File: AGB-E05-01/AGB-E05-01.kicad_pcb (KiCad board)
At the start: 2 copper layers, 51 x 31.1 mm, 24 parts, among them U0 CartBus, X1 Crystal_GND2

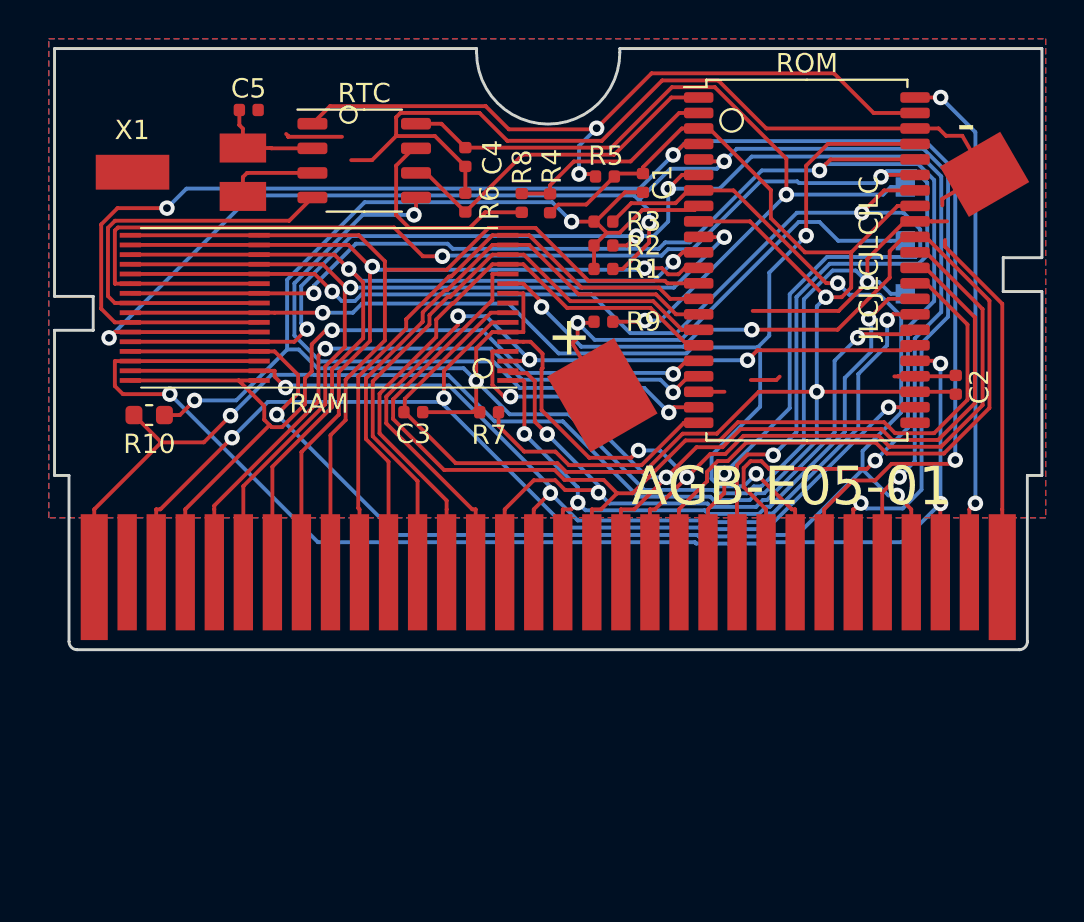
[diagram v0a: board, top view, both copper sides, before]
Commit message: Updated AGB-E05-01 to look more original
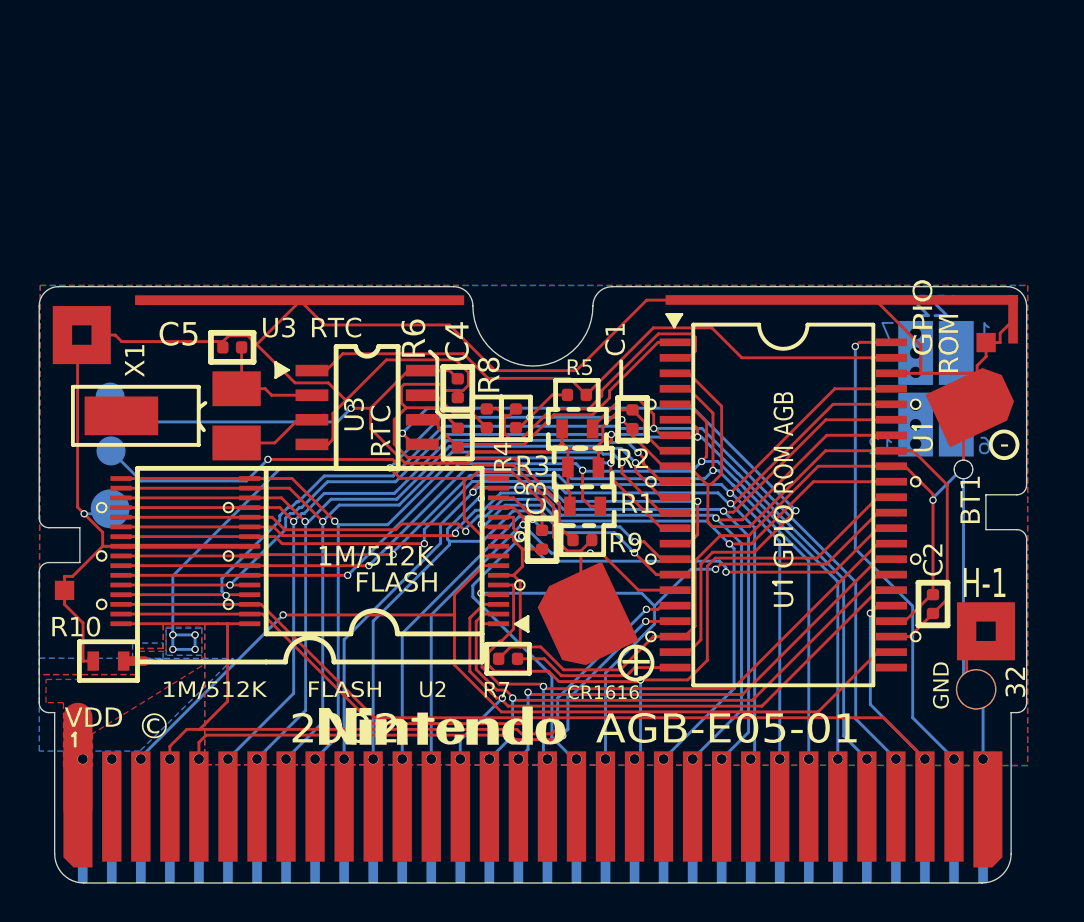
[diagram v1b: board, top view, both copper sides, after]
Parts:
- added A1: Date Indicator, HDR_Gameboy_Date_Indicators:06 June, B.Cu at (172.4, 88.2)
- added A2: 3x3Pad, HDR_Gameboy:3x3mm_Pad, F.Cu at (174.9, 100.7)
- added A3: 3x3Pad, HDR_Gameboy:3x3mm_Pad, F.Cu at (128.2, 85.4)
- added A4: 1x1Pad, HDR_Gameboy:1x1mm_Pad, F.Cu at (175.0, 85.8)
- added A5: 1x1Pad, HDR_Gameboy:1x1mm_Pad, F.Cu at (127.4, 98.6)
- added A6: CartBrow_Left, HDR_Gameboy:AGB-Cartbrow_Left, F.Cu at (139.5, 83.6)
- added A7: CartBrow_Right, HDR_Gameboy:AGB-Cartbrow_Right, F.Cu at (167.5, 83.6)
- added G1: Nintendo Logo, Custom:Nintendo-GBA-Logo, F.Cu at (146.9, 105.6)
- added PlatedHole1: MountingHole, Custom:TestPoint_Plated_Hole_D2.0mm, F.Cu at (174.4, 103.7)
- added kibuzzard-62A1ACD3: G***, kibuzzard-62A1ACD3, B.Cu at (130.4, 96.0)
- added kibuzzard-62A1AD16: G***, kibuzzard-62A1AD16, B.Cu at (131.6, 91.4)
- added kibuzzard-62A1AD21: G***, kibuzzard-62A1AD21, B.Cu at (131.6, 88.6)
- BT1: footprint NintendoFootprints:CR1616 -> HDR_Gameboy:AGB-CR1616
- C1, C2, C3, C4, C5: footprint Capacitor_SMD:C_0402_1005Metric -> HDR_Gameboy:AGB-C_0402
- R1, R2, R3: footprint Resistor_SMD:R_0402_1005Metric -> HDR_Gameboy:AGB-R-0603_OPT
- R10: footprint Resistor_SMD:R_0603_1608Metric -> HDR_Gameboy:AGB-R-0603
- R4, R5, R6, R7, R8, R9: footprint Resistor_SMD:R_0402_1005Metric -> HDR_Gameboy:AGB-R_0402
- TP1, TP2: footprint TestPoint:TestPoint_Pad_1.0x1.0mm -> HDR_Gameboy:AGB-Testpoint
- TP3: footprint TestPoint:TestPoint_Pad_1.0x1.0mm -> HDR_Gameboy:AGB-Testpoint_Ground
- U0: footprint NintendoFootprints:CartBus -> HDR_Gameboy:AGB_Cartridge
- U1: renamed from ROM; footprint Package_SO:TSOP-II-44_10.16x18.41mm_P0.8mm -> HDR_Gameboy:AGB-TSOP-II-44_10.16x18.41mm_P0.8mm
- U2: renamed from RAM; footprint NintendoFootprints:GBA-Flash -> HDR_Gameboy:AGB-TSOP-I-32
- U3: renamed from RTC; footprint Package_SO:SSOP-8_3.9x5.05mm_P1.27mm -> HDR_Gameboy:AGB-SSOP8
- X1: footprint NintendoFootprints:Crystal GBA -> HDR_Gameboy:AGB-Crystal
- moved TP3 42.5 mm to (129.7, 94.4)
- moved TP1 42.5 mm to (129.7, 88.6)
- moved TP2 42.5 mm to (129.8, 91.4)
- moved U0 27.8 mm to (151.5, 109.8)
- moved R10 12.9 mm to (129.6, 102.3), turned to 180 degrees
- moved R7 12.8 mm to (150.3, 102.1)
- moved U3 12.8 mm to (143.0, 89.2)
- moved U1 12.7 mm to (164.5, 94.2)
- moved X1 12.6 mm to (134.8, 89.6)
- moved U2 12.6 mm to (140.0, 96.6)
- moved BT1 12.4 mm to (164.7, 95.1), turned to 25 degrees
- moved R1 12.3 mm to (154.2, 94.3)
- moved C5 12.3 mm to (136.0, 86.0), turned to 0 degrees
- moved C1 12.2 mm to (156.7, 89.8), turned to 90 degrees
- moved R6 12.1 mm to (147.7, 90.7)
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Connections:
- net Net-(C4-Pad2) renamed VDD
- net Net-(C5-Pad2) renamed XIN
- net Net-(U3-Pad3) renamed XOUT
- net ~INT renamed INT
- C2 pad 1: +3V3 -> GND
- C2 pad 2: GND -> +3V3
- U0 pad 2: Net-(U0-Pad2) -> unconnected-(U0-Pad2)
- U1 pad 23: Net-(U1-Pad23) -> unconnected-(U1-Pad23)
- U2 pad 9: Net-(U2-Pad9) -> unconnected-(U2-Pad9)
- X1 pad 2: Net-(X1-Pad2) -> unconnected-(X1-Pad2)
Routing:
- net +3V3: track 133.5 -> 100.3 mm, vias 3 -> 7
- net D4: track 86.9 -> 56.3 mm, vias 3 -> 2
- net D5: track 86.5 -> 58.9 mm, vias 4 -> 3
- net D1: track 84.5 -> 58.0 mm, vias 3 -> 2
- net A15: track 58.6 -> 38.1 mm
- net D2: track 79.1 -> 58.8 mm, vias 3 -> 2
- net A12: track 56.5 -> 38.4 mm, vias 0 -> 2
- net D7: track 79.6 -> 64.0 mm, vias 3 -> 2
- net D0: track 73.4 -> 58.1 mm, vias 3 -> 2
- net D6: track 74.0 -> 59.3 mm, vias 4 -> 3
- net GND: track 208.4 -> 222.9 mm, vias 4 -> 3
- net A13: track 46.4 -> 34.1 mm
- net CS2: track 67.8 -> 55.5 mm, vias 3 -> 1
- net A14: track 47.0 -> 38.4 mm, vias 2 -> 1
- net A8: track 42.8 -> 34.3 mm, vias 3 -> 1
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- added copper zone on B.Cu, net +3V3
- added copper zone on F.Cu, net +3V3
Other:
- board size 51 x 31.1 mm -> 51 x 30.8 mm
- net class Default removed
- rule pad_to_mask_clearance: 0.0508 -> 0
- board text added: "1M/512K"
- board text added: "2002 AGB-E05-01"
- board text added: "32"
- board text added: "AGB"
- board text added: "BT1"
- board text added: "CR1616"
- board text added: "FLASH"
- board text added: "GND"
- board text added: "GPIO"
- board text added: "H-1"
- board text added: "ROM"
- board text added: "RTC"
- board text added: "U"
- board text added: "U3"
- board text added: "VDD"
- board text added: "©"
- board text removed: "AGB-E05-01"
- board text removed: "JLCJLCJLCJLC"
